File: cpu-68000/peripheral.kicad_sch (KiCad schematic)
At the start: 59 parts, among them J501 Conn_01x05_Male, J502 DB9_Male_MountingHoles, J503 Conn_02x03_Odd_Even, SW501 SW_DIP_x05, SW502 Blue, SW503 Black, U501 74HC2G14, U502 PCA9543A, U503 XR68C681, U504 PCF8584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

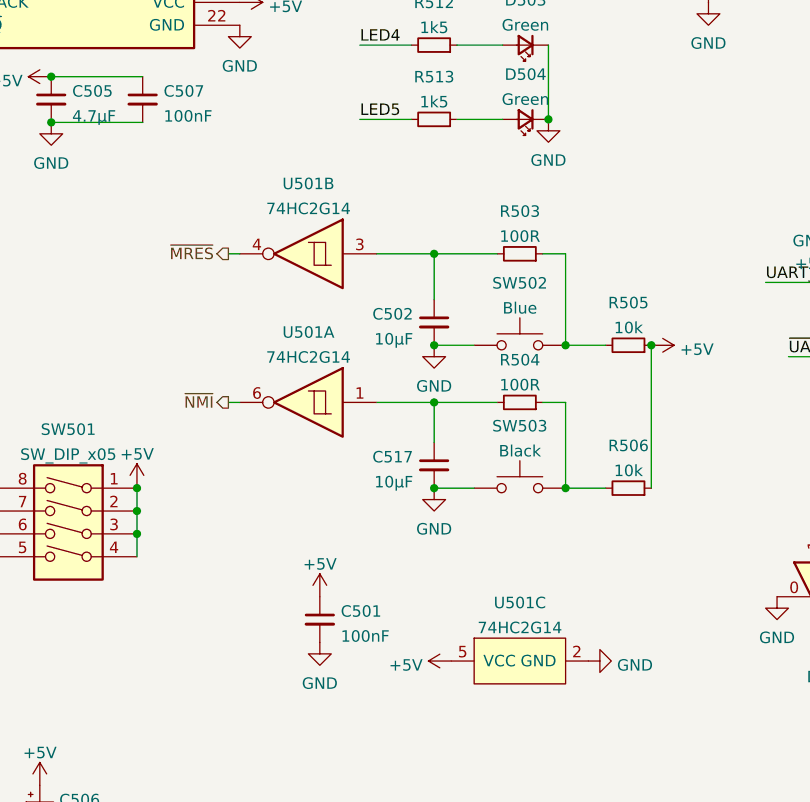
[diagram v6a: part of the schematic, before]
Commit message: Minor fixes for wrong parts
- Mostly an incorrect fuse value and the wrong type of buffer on the CPU
  board buttons
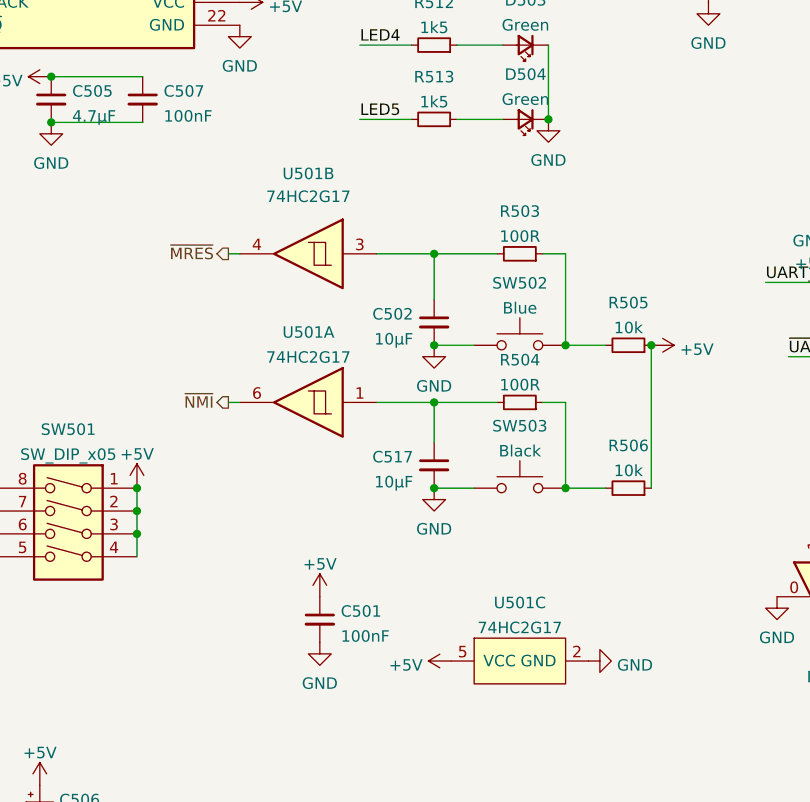
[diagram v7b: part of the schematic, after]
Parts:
- U501: value 74HC2G14 -> 74HC2G17; symbol 68komputer-common:74HC2G14 -> 68komputer-common:74HC2G17
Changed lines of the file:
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@@
     (pin "1")
   )
-  (symbol (lib_id "68komputer-common:74HC2G14") (at 198.755 114.3 0) (mirror y) (unit 2)
-    (in_bom yes) (on_board yes) (fields_autoplaced)
-    (property "Reference" "U501" (id 0) (at 198.755 106.5235 0))
-    (property "Value" "74HC2G14" (id 1) (at 198.755 109.2986 0))
-    (property "Footprint" "Package_SO:TSOP-6_1.65x3.05mm_P0.95mm" (id 2) (at 198.755 114.3 0)
+  (symbol (lib_id "68komputer-common:74HC2G17") (at 198.755 114.3 0) (mirror y) (unit 2)
+    (in_bom yes) (on_board yes) (fields_autoplaced)
+    (property "Reference" "U501" (id 0) (at 198.755 105.41 0))
+    (property "Value" "74HC2G17" (id 1) (at 198.755 107.95 0))
+    (property "Footprint" "Package_SO:TSOP-6_1.65x3.05mm_P0.95mm" (id 2) (at 198.755 109.22 0)
       (effects (font (size 1.27 1.27)) hide)
     )
@@
     (pin "1")
   )
-  (symbol (lib_id "68komputer-common:74HC2G14") (at 198.755 130.81 0) (mirror y) (unit 1)
+  (symbol (lib_id "68komputer-common:74HC2G17") (at 198.755 130.81 0) (mirror y) (unit 1)
     (in_bom yes) (on_board yes) (fields_autoplaced)
     (property "Reference" "U501" (id 0) (at 198.755 123.0335 0))
-    (property "Value" "74HC2G14" (id 1) (at 198.755 125.8086 0))
-    (property "Footprint" "Package_SO:TSOP-6_1.65x3.05mm_P0.95mm" (id 2) (at 198.755 130.81 0)
+    (property "Value" "74HC2G17" (id 1) (at 198.755 125.8086 0))
+    (property "Footprint" "Package_SO:TSOP-6_1.65x3.05mm_P0.95mm" (id 2) (at 198.755 125.73 0)
       (effects (font (size 1.27 1.27)) hide)
     )
@@
     (pin "1")
   )
-  (symbol (lib_id "68komputer-common:74HC2G14") (at 222.25 154.461 0) (unit 3)
+  (symbol (lib_id "68komputer-common:74HC2G17") (at 222.25 154.461 0) (unit 3)
     (in_bom yes) (on_board yes)
     (property "Reference" "U501" (id 0) (at 222.25 153.0853 0))
-    (property "Value" "74HC2G14" (id 1) (at 222.25 155.8604 0))
-    (property "Footprint" "Package_SO:TSOP-6_1.65x3.05mm_P0.95mm" (id 2) (at 222.25 154.461 0)
-      (effects (font (size 1.27 1.27)) hide)
-    )
+    (property "Value" "74HC2G17" (id 1) (at 222.25 155.8604 0))
+    (property "Footprint" "Package_SO:TSOP-6_1.65x3.05mm_P0.95mm" (id 2) (at 222.25 149.381 0)
+      (effects (font (size 1.27 1.27)) hide)
+    )

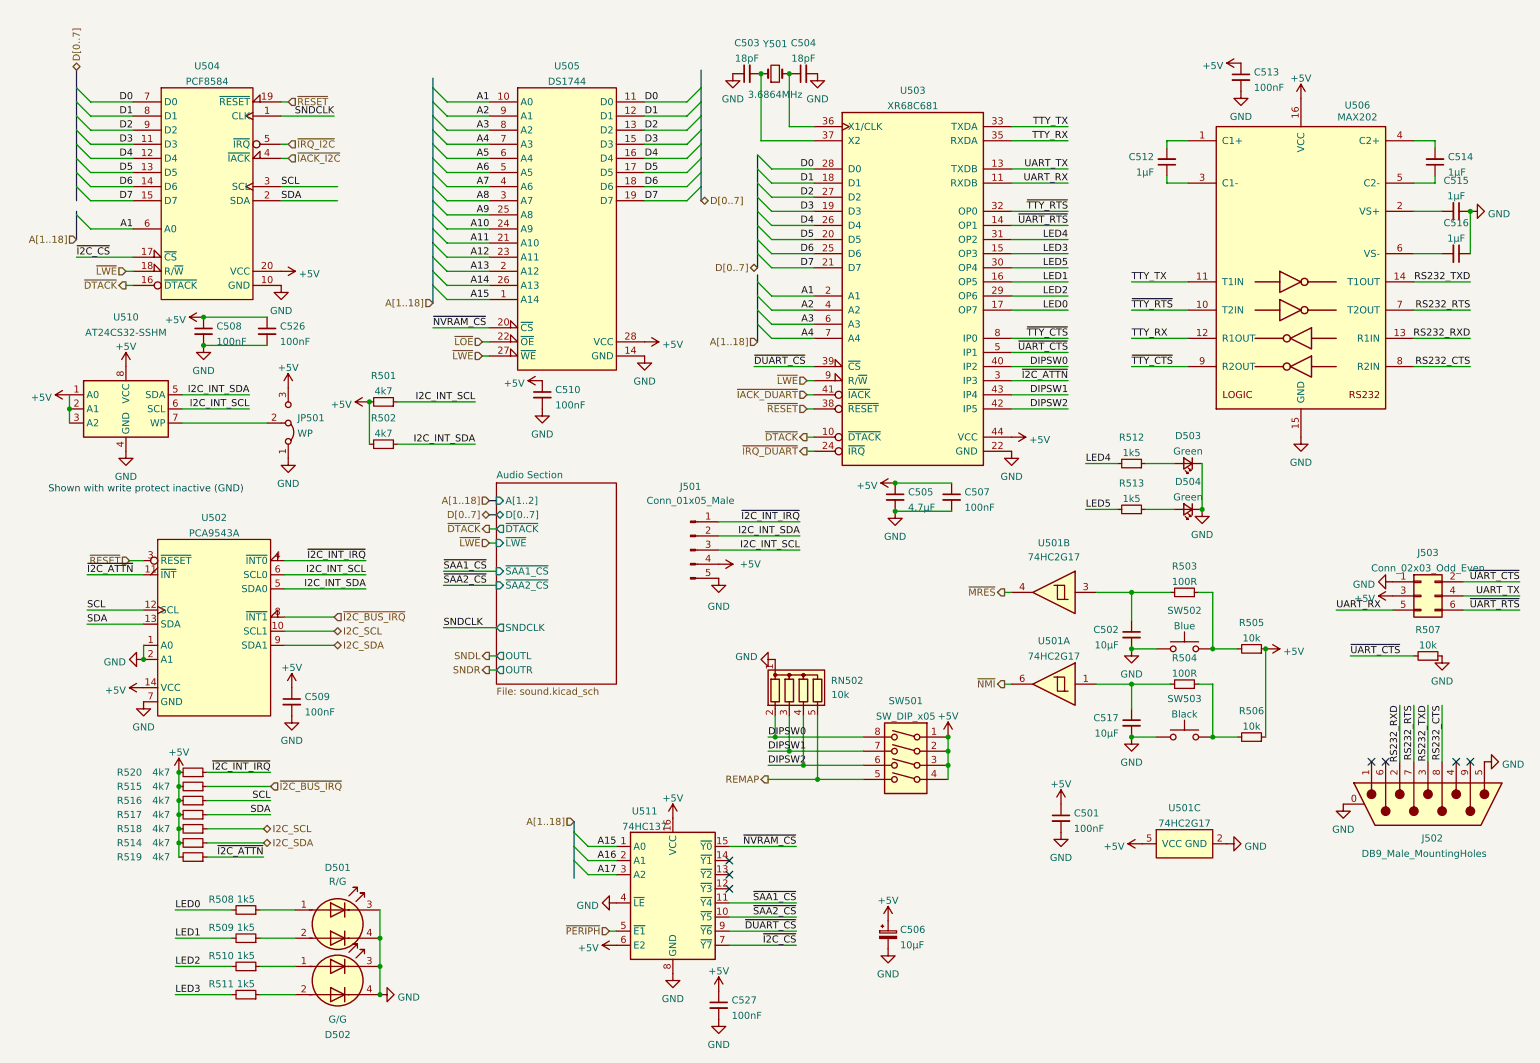
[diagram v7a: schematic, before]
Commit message: Start of rev 2 board
- This drops bus buffers, and replaces flash with DIP socketed versions.
  Also some minor tweaks to the board

- Fixed power LED (D201) positioning

- Fixed LED (too dark) for the right angle indicators
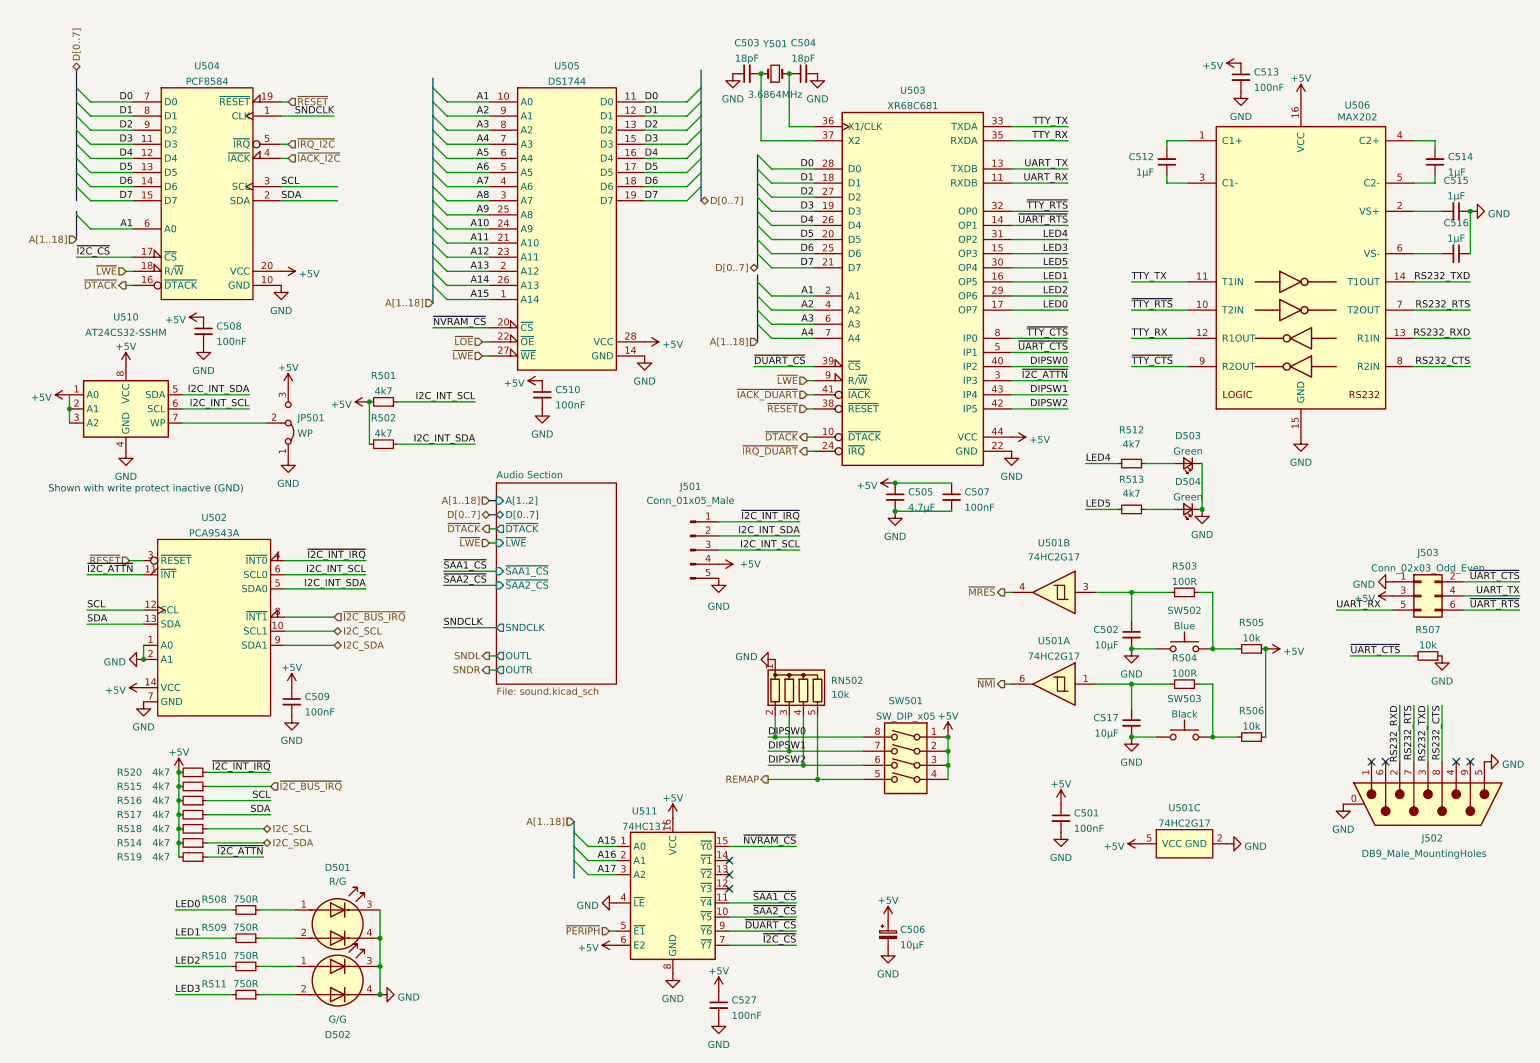
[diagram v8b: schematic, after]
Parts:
- removed C526: 100nF, Capacitor_SMD:C_0805_2012Metric, symbol Device:C_Small
- R508, R509, R510, R511: value 1k5 -> 750R
- R512, R513: value 1k5 -> 4k7
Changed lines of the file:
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@@
   (title_block
     (title "68komputer CPU Board")
-    (date "2021-12-11")
-    (rev "1")
+    (date "2021-12-30")
+    (rev "2")
     (company "Tristan Seifert")
     (comment 1 "PCF8584 clk is not quite 8MHz; I²C clocks will be incorrect")
@@
   (junction (at 77.47 176.53) (diameter 0) (color 0 0 0 0)
   )
-  (junction (at 45.72 64.77) (diameter 0) (color 0 0 0 0)
-  )
   (junction (at 151.13 20.955) (diameter 0) (color 0 0 0 0)
   )
@@
   (junction (at 179.705 142.875) (diameter 0) (color 0 0 0 0)
   )
-  (junction (at 45.72 69.85) (diameter 0) (color 0 0 0 0)
-  )
   (junction (at 170.18 99.695) (diameter 0) (color 0 0 0 0)
   )
@@
     (stroke (width 0) (type default) (color 0 0 0 0))
   )
-  (wire (pts (xy 45.72 69.85) (xy 57.15 69.85))
-    (stroke (width 0) (type default) (color 0 0 0 0))
-  )
   (wire (pts (xy 138.43 104.14) (xy 153.035 104.14))
     (stroke (width 0) (type default) (color 0 0 0 0))
@@
     (stroke (width 0) (type default) (color 0 0 0 0))
   )
-  (wire (pts (xy 45.72 64.77) (xy 57.15 64.77))
-    (stroke (width 0) (type default) (color 0 0 0 0))
-  )
   (wire (pts (xy 97.155 102.87) (xy 98.425 102.87))
     (stroke (width 0) (type default) (color 0 0 0 0))
@@
     (pin "1")
   )
-  (symbol (lib_id "Device:C_Small") (at 57.15 67.31 0) (unit 1)
-    (in_bom yes) (on_board yes) (fields_autoplaced)
-    (property "Reference" "C526" (id 0) (at 59.4741 66.4015 0)
-      (effects (font (size 1.27 1.27)) (justify left))
-    )
-    (property "Value" "100nF" (id 1) (at 59.4741 69.1766 0)
-      (effects (font (size 1.27 1.27)) (justify left))
-    )
-    (property "Footprint" "Capacitor_SMD:C_0805_2012Metric" (id 2) (at 57.15 67.31 0)
-      (effects (font (size 1.27 1.27)) hide)
-    )
-    (property "Datasheet" "~" (id 3) (at 57.15 67.31 0)
-      (effects (font (size 1.27 1.27)) hide)
-    )
-    (pin "1")
-    (pin "2")
-  )
   (symbol (lib_id "power:+5V") (at 200.025 152.4 0) (unit 1)
     (in_bom yes) (on_board yes) (fields_autoplaced)
@@
   (symbol (lib_id "Device:R_Small") (at 53.34 186.69 270) (mirror x) (unit 1)
     (in_bom yes) (on_board yes)
-    (property "Reference" "R511" (id 0) (at 48.895 184.785 90))
-    (property "Value" "1k5" (id 1) (at 53.34 184.762 90))
+    (property "Reference" "R511" (id 0) (at 47.625 184.785 90))
+    (property "Value" "750R" (id 1) (at 53.34 184.762 90))
     (property "Footprint" "Resistor_SMD:R_0805_2012Metric" (id 2) (at 53.34 186.69 0)
       (effects (font (size 1.27 1.27)) hide)
@@
   (symbol (lib_id "Device:R_Small") (at 53.34 181.61 270) (mirror x) (unit 1)
     (in_bom yes) (on_board yes)
-    (property "Reference" "R510" (id 0) (at 48.895 179.705 90))
-    (property "Value" "1k5" (id 1) (at 53.34 179.682 90))
+    (property "Reference" "R510" (id 0) (at 47.625 179.705 90))
+    (property "Value" "750R" (id 1) (at 53.34 179.682 90))
     (property "Footprint" "Resistor_SMD:R_0805_2012Metric" (id 2) (at 53.34 181.61 0)
       (effects (font (size 1.27 1.27)) hide)
@@
   (symbol (lib_id "Device:R_Small") (at 212.725 91.1074 270) (mirror x) (unit 1)
     (in_bom yes) (on_board yes) (fields_autoplaced)
-    (property "Reference" "R512" (id 0) (at 212.725 86.4043 90))
-    (property "Value" "1k5" (id 1) (at 212.725 89.1794 90))
+    (property "Reference" "R512" (id 0) (at 212.725 85.09 90))
+    (property "Value" "4k7" (id 1) (at 212.725 87.63 90))
     (property "Footprint" "Resistor_SMD:R_0805_2012Metric" (id 2) (at 212.725 91.1074 0)
       (effects (font (size 1.27 1.27)) hide)
@@
   (symbol (lib_id "Device:R_Small") (at 53.34 171.45 270) (mirror x) (unit 1)
     (in_bom yes) (on_board yes)
-    (property "Reference" "R508" (id 0) (at 48.895 169.545 90))
-    (property "Value" "1k5" (id 1) (at 53.34 169.522 90))
+    (property "Reference" "R508" (id 0) (at 47.625 169.545 90))
+    (property "Value" "750R" (id 1) (at 53.34 169.522 90))
     (property "Footprint" "Resistor_SMD:R_0805_2012Metric" (id 2) (at 53.34 171.45 0)
       (effects (font (size 1.27 1.27)) hide)
@@
   (symbol (lib_id "Device:R_Small") (at 212.725 99.3624 270) (mirror x) (unit 1)
     (in_bom yes) (on_board yes) (fields_autoplaced)
-    (property "Reference" "R513" (id 0) (at 212.725 94.6593 90))
-    (property "Value" "1k5" (id 1) (at 212.725 97.4344 90))
+    (property "Reference" "R513" (id 0) (at 212.725 93.98 90))
+    (property "Value" "4k7" (id 1) (at 212.725 96.52 90))
     (property "Footprint" "Resistor_SMD:R_0805_2012Metric" (id 2) (at 212.725 99.3624 0)
       (effects (font (size 1.27 1.27)) hide)
@@
   (symbol (lib_id "Device:R_Small") (at 53.34 176.53 270) (mirror x) (unit 1)
     (in_bom yes) (on_board yes)
-    (property "Reference" "R509" (id 0) (at 48.895 174.625 90))
-    (property "Value" "1k5" (id 1) (at 53.34 174.602 90))
+    (property "Reference" "R509" (id 0) (at 47.625 174.625 90))
+    (property "Value" "750R" (id 1) (at 53.34 174.602 90))
     (property "Footprint" "Resistor_SMD:R_0805_2012Metric" (id 2) (at 53.34 176.53 0)
       (effects (font (size 1.27 1.27)) hide)
